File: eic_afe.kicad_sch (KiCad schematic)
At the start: 16 parts, among them J10 132134, J2 878311420, J3 132134, J4 132134, J5 132134, J6 132134, J7 132134, J8 132134, J9 132134

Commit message: Change SMA to edge-launch
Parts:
- removed J10, J3, J4, J5, J6, J7, J8, J9: 132134, My_Footprints:SMA_Amphenol_132134_Vertical, symbol My_Symbols:SMA-Straight-132134
- added J10, J3, J4, J5, J6, J7, J8, J9: 132289, Connector_Coaxial:SMA_Amphenol_132289_EdgeMount, symbol My_Symbols:SMA-edge-132289
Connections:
- net Channel B/atten_clk is gone; now on net Channel A/atten_clk: R7.2
- net Channel A/rf_in: now also J3.1 (In)
- net Channel A/rf_out: now also J4.1 (In)
- net Channel B/rf_in: now also J5.1 (In)
- net Channel B/rf_out: now also J6.1 (In)
- net Channel C/rf_in: now also J7.1 (In)
- net Channel C/rf_out: now also J8.1 (In)
- net Channel D/rf_in: now also J9.1 (In)
- net Channel D/rf_out: now also J10.1 (In)
- net GND: now also J10.2 (Ext), J3.2 (Ext), J4.2 (Ext), J5.2 (Ext), J6.2 (Ext), J7.2 (Ext), J8.2 (Ext), J9.2 (Ext)

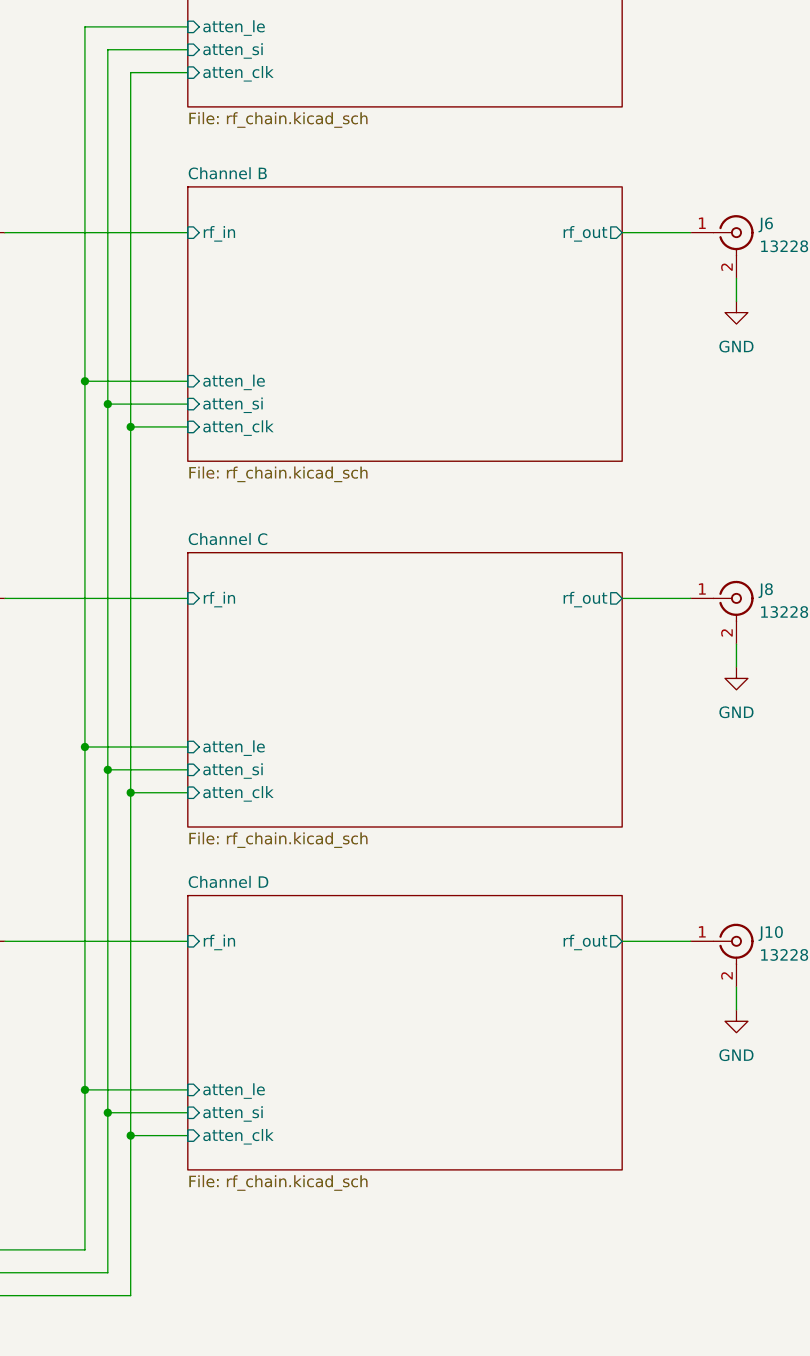
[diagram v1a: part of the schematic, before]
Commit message: Finish preliminary routing of one channel
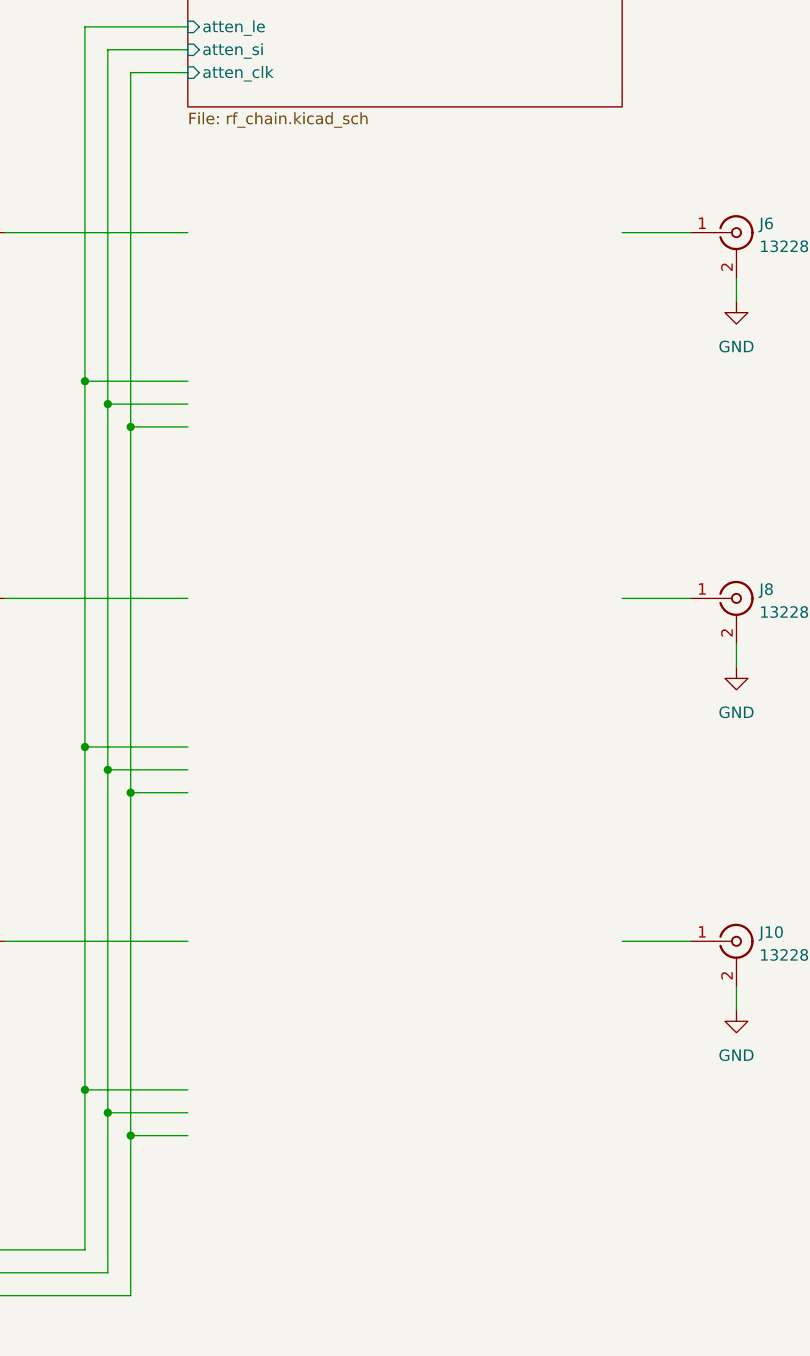
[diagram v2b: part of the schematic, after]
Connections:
- net Channel B/rf_in: no longer names the net of J5.1 (In)
- net Channel B/rf_out: no longer names the net of J6.1 (In)
- net Channel C/rf_in: no longer names the net of J7.1 (In)
- net Channel C/rf_out: no longer names the net of J8.1 (In)
- net Channel D/rf_in: no longer names the net of J9.1 (In)
- net Channel D/rf_out: no longer names the net of J10.1 (In)
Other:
- removed sheet Channel B
- removed sheet Channel C
- removed sheet Channel D

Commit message: Add part numbers for BOM
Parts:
- J10, J3, J4, J5, J6, J7, J8, J9: MFG (none) -> Amphenol RF; MFG_PN (none) -> 132289; Price (none) -> 7.25
- J2: MFG MOLEX -> Molex; Price (none) -> 1.84
- R5, R6, R7: MFG (none) -> Panasonic; MFG_PN (none) -> ERJ-3EKF2202V

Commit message: Update RF shield
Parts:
- added SH1: RFShield_TwoPieces, My_Footprints:RF_Shield_Rev6_Footprint, symbol Device:RFShield_TwoPieces
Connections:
- net GND: now also SH1.1 (Shield)
